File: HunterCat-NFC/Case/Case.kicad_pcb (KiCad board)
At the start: 2 copper layers, 209.4 x 35.2 mm, 4 parts

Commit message: select case
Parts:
- moved REF** 86.6 mm to (177.5, 103.8)
- moved REF** 86.3 mm to (177.2, 77.5)
- moved REF** 37.6 mm to (252.9, 77.2)
- moved REF** 36.9 mm to (252.3, 103.6)
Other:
- board size 209.4 x 35.2 mm -> 84.9 x 34.5 mm
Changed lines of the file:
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@@
-(kicad_pcb (version 20171130) (host pcbnew "(5.1.6)-1")
+(kicad_pcb (version 20171130) (host pcbnew "(5.1.5-0-10_14)")
   (general
     (thickness 1.6)
-    (drawings 44)
+    (drawings 34)
     (tracks 2)
     (zones 0)
@@
     (43 Eco2.User user)
     (44 Edge.Cuts user)
-    (45 Margin user hide)
+    (45 Margin user)
     (46 B.CrtYd user)
     (47 F.CrtYd user)
@@
   )
   (module MountingHole:MountingHole_3.2mm_M3 (layer F.Cu)
-    (at 90.91 79.29)
-    (descr "Mounting Hole 3.2mm, no annular, M3")
-    (tags "mounting hole 3.2mm no annular m3")
-    (attr virtual)
-    (fp_text reference REF** (at 0 -4.2) (layer F.Fab)
-      (effects (font (size 1 1) (thickness 0.15)))
-    )
-    (fp_text value MountingHole_3.2mm_M3 (at 0 4.2) (layer F.Fab)
-      (effects (font (size 1 1) (thickness 0.15)))
-    )
-    (fp_circle (center 0 0) (end 3.45 0) (layer F.CrtYd) (width 0.05))
-    (fp_circle (center 0 0) (end 3.2 0) (layer Cmts.User) (width 0.15))
-    (fp_text user %R (at 0.3 0) (layer F.Fab)
-      (effects (font (size 1 1) (thickness 0.15)))
-    )
-    (pad 1 np_thru_hole circle (at 0 0) (size 3.2 3.2) (drill 3.2) (layers *.Cu *.Mask))
-  )
-  (module MountingHole:MountingHole_3.2mm_M3 (layer F.Cu)
-    (at 90.91 102.76)
-    (descr "Mounting Hole 3.2mm, no annular, M3")
-    (tags "mounting hole 3.2mm no annular m3")
-    (attr virtual)
-    (fp_text reference REF** (at 0 -4.2) (layer F.Fab)
-      (effects (font (size 1 1) (thickness 0.15)))
-    )
-    (fp_text value MountingHole_3.2mm_M3 (at 0 4.2) (layer F.Fab)
-      (effects (font (size 1 1) (thickness 0.15)))
-    )
-    (fp_circle (center 0 0) (end 3.45 0) (layer F.CrtYd) (width 0.05))
-    (fp_circle (center 0 0) (end 3.2 0) (layer Cmts.User) (width 0.15))
-    (fp_text user %R (at 0.3 0) (layer F.Fab)
-      (effects (font (size 1 1) (thickness 0.15)))
-    )
-    (pad 1 np_thru_hole circle (at 0 0) (size 3.2 3.2) (drill 3.2) (layers *.Cu *.Mask))
-  )
-  (module MountingHole:MountingHole_3.2mm_M3 (layer F.Cu)
-    (at 215.42 102.08)
-    (descr "Mounting Hole 3.2mm, no annular, M3")
-    (tags "mounting hole 3.2mm no annular m3")
-    (attr virtual)
-    (fp_text reference REF** (at 0 -4.2) (layer F.Fab)
-      (effects (font (size 1 1) (thickness 0.15)))
-    )
-    (fp_text value MountingHole_3.2mm_M3 (at 0 4.2) (layer F.Fab)
-      (effects (font (size 1 1) (thickness 0.15)))
-    )
-    (fp_text user %R (at 0.3 0) (layer F.Fab)
-      (effects (font (size 1 1) (thickness 0.15)))
-    )
-    (fp_circle (center 0 0) (end 3.2 0) (layer Cmts.User) (width 0.15))
-    (fp_circle (center 0 0) (end 3.45 0) (layer F.CrtYd) (width 0.05))
-    (pad 1 np_thru_hole circle (at 0 0) (size 3.2 3.2) (drill 3.2) (layers *.Cu *.Mask))
-  )
-  (module MountingHole:MountingHole_3.2mm_M3 (layer F.Cu)
-    (at 215.42 78.61)
-    (descr "Mounting Hole 3.2mm, no annular, M3")
-    (tags "mounting hole 3.2mm no annular m3")
-    (attr virtual)
-    (fp_text reference REF** (at 0 -4.2) (layer F.Fab)
-      (effects (font (size 1 1) (thickness 0.15)))
-    )
-    (fp_text value MountingHole_3.2mm_M3 (at 0 4.2) (layer F.Fab)
-      (effects (font (size 1 1) (thickness 0.15)))
-    )
-    (fp_text user %R (at 0.3 0) (layer F.Fab)
-      (effects (font (size 1 1) (thickness 0.15)))
-    )
-    (fp_circle (center 0 0) (end 3.2 0) (layer Cmts.User) (width 0.15))
-    (fp_circle (center 0 0) (end 3.45 0) (layer F.CrtYd) (width 0.05))
-    (pad 1 np_thru_hole circle (at 0 0) (size 3.2 3.2) (drill 3.2) (layers *.Cu *.Mask))
-  )
-  (gr_line (start 60.26 73.79) (end 70.27 73.79) (layer Edge.Cuts) (width 0.05))
-  (gr_arc (start 52.06 104.29) (end 48.06 104.29) (angle -90) (layer Edge.Cuts) (width 0.05))
-  (gr_arc (start 128.95 77.79) (end 132.95 77.79) (angle -90) (layer Edge.Cuts) (width 0.05))
-  (gr_arc (start 128.95 104.29) (end 128.959999 108.289999) (angle -90) (layer Edge.Cuts) (width 0.05))
-  (gr_line (start 52.06 108.29) (end 128.959999 108.289999) (layer Edge.Cuts) (width 0.05))
-  (gr_line (start 128.95 73.79) (end 70.27 73.79) (layer Edge.Cuts) (width 0.05))
-  (gr_line (start 132.949999 104.280001) (end 132.95 77.79) (layer Edge.Cuts) (width 0.05))
-  (gr_arc (start 52.05 77.78) (end 52.05 73.79) (angle -90) (layer Edge.Cuts) (width 0.05))
-  (gr_line (start 48.06 104.29) (end 48.06 77.78) (layer Edge.Cuts) (width 0.05))
-  (gr_line (start 60.26 73.79) (end 52.05 73.79) (layer Edge.Cuts) (width 0.05))
+    (at 177.24 77.46)
+    (descr "Mounting Hole 3.2mm, no annular, M3")
+    (tags "mounting hole 3.2mm no annular m3")
+    (attr virtual)
+    (fp_text reference REF** (at 0 -4.2) (layer F.Fab)
+      (effects (font (size 1 1) (thickness 0.15)))
+    )
+    (fp_text value MountingHole_3.2mm_M3 (at 0 4.2) (layer F.Fab)
+      (effects (font (size 1 1) (thickness 0.15)))
+    )
+    (fp_circle (center 0 0) (end 3.45 0) (layer F.CrtYd) (width 0.05))
+    (fp_circle (center 0 0) (end 3.2 0) (layer Cmts.User) (width 0.15))
+    (fp_text user %R (at 0.3 0) (layer F.Fab)
+      (effects (font (size 1 1) (thickness 0.15)))
+    )
+    (pad 1 np_thru_hole circle (at 0 0) (size 3.2 3.2) (drill 3.2) (layers *.Cu *.Mask))
+  )
+  (module MountingHole:MountingHole_3.2mm_M3 (layer F.Cu)
+    (at 177.46 103.8)
+    (descr "Mounting Hole 3.2mm, no annular, M3")
+    (tags "mounting hole 3.2mm no annular m3")
+    (attr virtual)
+    (fp_text reference REF** (at 0 -4.2) (layer F.Fab)
+      (effects (font (size 1 1) (thickness 0.15)))
+    )
+    (fp_text value MountingHole_3.2mm_M3 (at 0 4.2) (layer F.Fab)
+      (effects (font (size 1 1) (thickness 0.15)))
+    )
+    (fp_circle (center 0 0) (end 3.45 0) (layer F.CrtYd) (width 0.05))
+    (fp_circle (center 0 0) (end 3.2 0) (layer Cmts.User) (width 0.15))
+    (fp_text user %R (at 0.3 0) (layer F.Fab)
+      (effects (font (size 1 1) (thickness 0.15)))
+    )
+    (pad 1 np_thru_hole circle (at 0 0) (size 3.2 3.2) (drill 3.2) (layers *.Cu *.Mask))
+  )
+  (module MountingHole:MountingHole_3.2mm_M3 (layer F.Cu)
+    (at 252.28 103.58)
+    (descr "Mounting Hole 3.2mm, no annular, M3")
+    (tags "mounting hole 3.2mm no annular m3")
+    (attr virtual)
+    (fp_text reference REF** (at 0 -4.2) (layer F.Fab)
+      (effects (font (size 1 1) (thickness 0.15)))
+    )
+    (fp_text value MountingHole_3.2mm_M3 (at 0 4.2) (layer F.Fab)
+      (effects (font (size 1 1) (thickness 0.15)))
+    )
+    (fp_text user %R (at 0.3 0) (layer F.Fab)
+      (effects (font (size 1 1) (thickness 0.15)))
+    )
+    (fp_circle (center 0 0) (end 3.2 0) (layer Cmts.User) (width 0.15))
+    (fp_circle (center 0 0) (end 3.45 0) (layer F.CrtYd) (width 0.05))
+    (pad 1 np_thru_hole circle (at 0 0) (size 3.2 3.2) (drill 3.2) (layers *.Cu *.Mask))
+  )
+  (module MountingHole:MountingHole_3.2mm_M3 (layer F.Cu)
+    (at 252.95 77.23)
+    (descr "Mounting Hole 3.2mm, no annular, M3")
+    (tags "mounting hole 3.2mm no annular m3")
+    (attr virtual)
+    (fp_text reference REF** (at 0 -4.2) (layer F.Fab)
+      (effects (font (size 1 1) (thickness 0.15)))
+    )
+    (fp_text value MountingHole_3.2mm_M3 (at 0 4.2) (layer F.Fab)
+      (effects (font (size 1 1) (thickness 0.15)))
+    )
+    (fp_text user %R (at 0.3 0) (layer F.Fab)
+      (effects (font (size 1 1) (thickness 0.15)))
+    )
+    (fp_circle (center 0 0) (end 3.2 0) (layer Cmts.User) (width 0.15))
+    (fp_circle (center 0 0) (end 3.45 0) (layer F.CrtYd) (width 0.05))
+    (pad 1 np_thru_hole circle (at 0 0) (size 3.2 3.2) (drill 3.2) (layers *.Cu *.Mask))
+  )
   (dimension 5.5 (width 0.12) (layer Margin)
     (gr_text "5,500 mm" (at 285.49 104.86 90) (layer Margin)
@@
   )
   (dimension 50.760001 (width 0.12) (layer Margin)
-    (gr_text "50,760 mm" (at 232.06384 162.504943 360) (layer Margin)
-      (effects (font (size 1 1) (thickness 0.15)))
-    )
+    (gr_text "50,760 mm" (at 232.06384 162.504943) (layer Margin)
+      (effects (font (size 1 1) (thickness 0.15)))
+    )

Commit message: New Case
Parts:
- removed the REF** at (177.2, 77.5)
- removed the REF** at (177.5, 103.8)
- removed the REF** at (252.3, 103.6)
- removed the REF** at (252.9, 77.2)
- added REF**: MountingHole_2.2mm_M2, MountingHole:MountingHole_2.2mm_M2, F.Cu at (106.6, 143.0)
- added REF**: MountingHole_2.2mm_M2, MountingHole:MountingHole_2.2mm_M2, F.Cu at (188.5, 78.4)
- added REF**: MountingHole_2.2mm_M2, MountingHole:MountingHole_2.2mm_M2, F.Cu at (187.6, 143.0)
- added REF**: MountingHole_2.2mm_M2, MountingHole:MountingHole_2.2mm_M2, F.Cu at (187.8, 115.3)
- added REF**: MountingHole_2.2mm_M2, MountingHole:MountingHole_2.2mm_M2, F.Cu at (106.6, 115.3)
- added REF**: MountingHole_2.2mm_M2, MountingHole:MountingHole_2.2mm_M2, F.Cu at (138.2, 82.7)
- added REF**: MountingHole_2.2mm_M2, MountingHole:MountingHole_2.2mm_M2, F.Cu at (138.2, 104.0)
- added REF**: MountingHole_2.2mm_M2, MountingHole:MountingHole_2.2mm_M2, F.Cu at (107.3, 106.1)
- added REF**: MountingHole_2.2mm_M2, MountingHole:MountingHole_2.2mm_M2, F.Cu at (107.3, 78.4)
- added REF**: MountingHole_2.2mm_M2, MountingHole:MountingHole_2.2mm_M2, F.Cu at (188.2, 106.1)
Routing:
- net (no net): vias 2 -> 0
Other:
- board size 84.9 x 34.5 mm -> 88.7 x 70.4 mm

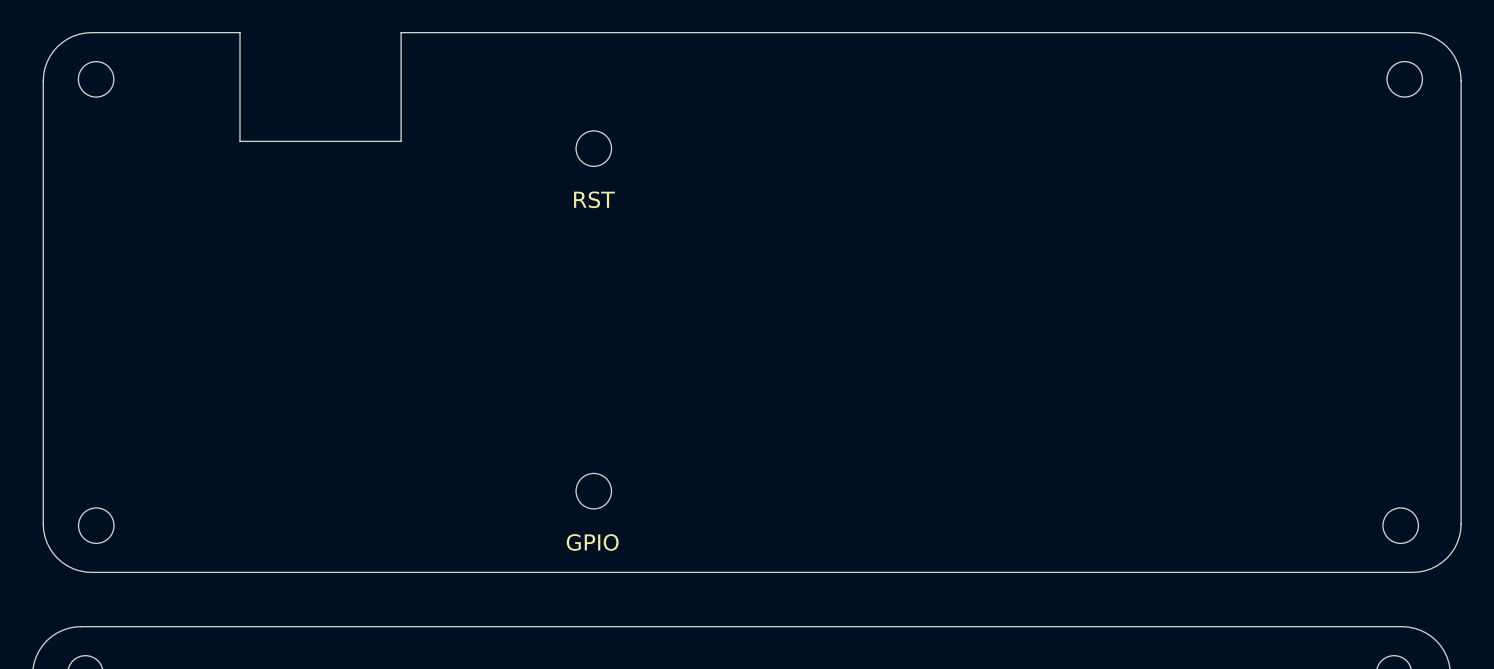
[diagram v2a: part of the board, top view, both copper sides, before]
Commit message: Add button
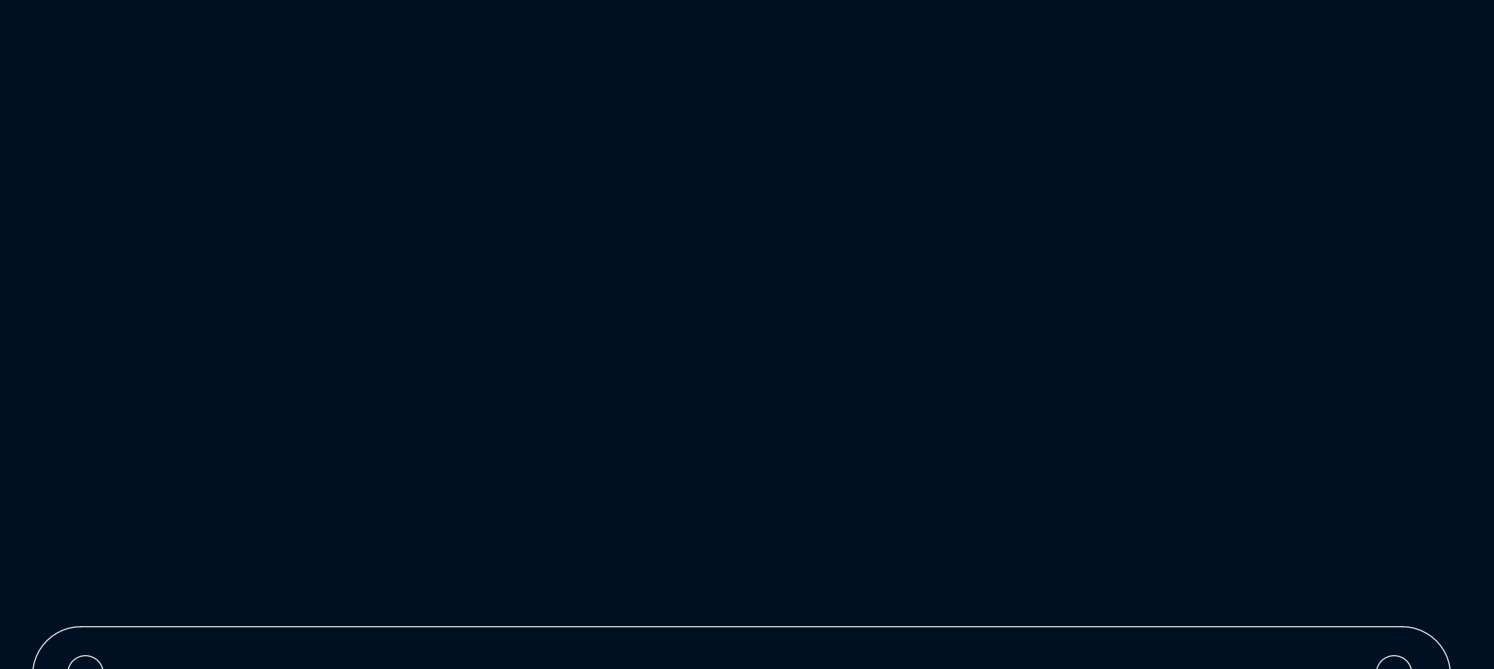
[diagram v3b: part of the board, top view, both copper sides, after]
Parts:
- removed the REF** at (188.5, 78.4)
- removed the REF** at (138.2, 82.7)
- removed the REF** at (138.2, 104.0)
- removed the REF** at (107.3, 106.1)
- removed the REF** at (107.3, 78.4)
- removed the REF** at (188.2, 106.1)
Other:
- board size 88.7 x 70.4 mm -> 88 x 33.5 mm
- board text removed: "GPIO"
- board text removed: "RST"
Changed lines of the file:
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@@
   (general
     (thickness 1.6)
-    (drawings 25)
+    (drawings 11)
     (tracks 0)
     (zones 0)
-    (modules 10)
+    (modules 4)
     (nets 1)
   )
@@
       (effects (font (size 1 1) (thickness 0.15)))
     )
-    (fp_text user %R (at 0.3 0) (layer F.Fab)
-      (effects (font (size 1 1) (thickness 0.15)))
-    )
-    (fp_circle (center 0 0) (end 2.2 0) (layer Cmts.User) (width 0.15))
-    (fp_circle (center 0 0) (end 2.45 0) (layer F.CrtYd) (width 0.05))
+    (fp_circle (center 0 0) (end 2.45 0) (layer F.CrtYd) (width 0.05))
+    (fp_circle (center 0 0) (end 2.2 0) (layer Cmts.User) (width 0.15))
+    (fp_text user %R (at 0.3 0) (layer F.Fab)
+      (effects (font (size 1 1) (thickness 0.15)))
+    )
     (pad 1 np_thru_hole circle (at 0 0) (size 2.2 2.2) (drill 2.2) (layers *.Cu *.Mask))
   )
@@
       (effects (font (size 1 1) (thickness 0.15)))
     )
-    (fp_text user %R (at 0.3 0) (layer F.Fab)
-      (effects (font (size 1 1) (thickness 0.15)))
-    )
-    (fp_circle (center 0 0) (end 2.2 0) (layer Cmts.User) (width 0.15))
-    (fp_circle (center 0 0) (end 2.45 0) (layer F.CrtYd) (width 0.05))
+    (fp_circle (center 0 0) (end 2.45 0) (layer F.CrtYd) (width 0.05))
+    (fp_circle (center 0 0) (end 2.2 0) (layer Cmts.User) (width 0.15))
+    (fp_text user %R (at 0.3 0) (layer F.Fab)
+      (effects (font (size 1 1) (thickness 0.15)))
+    )
     (pad 1 np_thru_hole circle (at 0 0) (size 2.2 2.2) (drill 2.2) (layers *.Cu *.Mask))
   )
@@
       (effects (font (size 1 1) (thickness 0.15)))
     )
-    (fp_circle (center 0 0) (end 2.45 0) (layer F.CrtYd) (width 0.05))
-    (fp_circle (center 0 0) (end 2.2 0) (layer Cmts.User) (width 0.15))
+    (fp_circle (center 0 0) (end 2.2 0) (layer Cmts.User) (width 0.15))
+    (fp_circle (center 0 0) (end 2.45 0) (layer F.CrtYd) (width 0.05))
     (fp_text user %R (at 0.3 0) (layer F.Fab)
       (effects (font (size 1 1) (thickness 0.15)))
@@
       (effects (font (size 1 1) (thickness 0.15)))
     )
-    (fp_circle (center 0 0) (end 2.45 0) (layer F.CrtYd) (width 0.05))
-    (fp_circle (center 0 0) (end 2.2 0) (layer Cmts.User) (width 0.15))
-    (fp_text user %R (at 0.3 0) (layer F.Fab)
-      (effects (font (size 1 1) (thickness 0.15)))
-    )
-    (pad 1 np_thru_hole circle (at 0 0) (size 2.2 2.2) (drill 2.2) (layers *.Cu *.Mask))
-  )
-  (module MountingHole:MountingHole_2.2mm_M2 (layer F.Cu)
-    (at 138.17 82.7)
-    (descr "Mounting Hole 2.2mm, no annular, M2")
-    (tags "mounting hole 2.2mm no annular m2")
-    (attr virtual)
-    (fp_text reference REF** (at 0 -3.2) (layer F.Fab)
-      (effects (font (size 1 1) (thickness 0.15)))
-    )
-    (fp_text value MountingHole_2.2mm_M2 (at 0 3.2) (layer F.Fab)
-      (effects (font (size 1 1) (thickness 0.15)))
-    )
-    (fp_text user %R (at 0.3 0) (layer F.Fab)
-      (effects (font (size 1 1) (thickness 0.15)))
-    )
-    (fp_circle (center 0 0) (end 2.2 0) (layer Cmts.User) (width 0.15))
-    (fp_circle (center 0 0) (end 2.45 0) (layer F.CrtYd) (width 0.05))
-    (pad 1 np_thru_hole circle (at 0 0) (size 2.2 2.2) (drill 2.2) (layers *.Cu *.Mask))
-  )
-  (module MountingHole:MountingHole_2.2mm_M2 (layer F.Cu)
-    (at 138.17 103.96)
-    (descr "Mounting Hole 2.2mm, no annular, M2")
-    (tags "mounting hole 2.2mm no annular m2")
-    (attr virtual)
-    (fp_text reference REF** (at 0 -3.2) (layer F.Fab)
-      (effects (font (size 1 1) (thickness 0.15)))
-    )
-    (fp_text value MountingHole_2.2mm_M2 (at 0 3.2) (layer F.Fab)
-      (effects (font (size 1 1) (thickness 0.15)))
-    )
-    (fp_circle (center 0 0) (end 2.45 0) (layer F.CrtYd) (width 0.05))
-    (fp_circle (center 0 0) (end 2.2 0) (layer Cmts.User) (width 0.15))
-    (fp_text user %R (at 0.3 0) (layer F.Fab)
-      (effects (font (size 1 1) (thickness 0.15)))
-    )
-    (pad 1 np_thru_hole circle (at 0 0) (size 2.2 2.2) (drill 2.2) (layers *.Cu *.Mask))
-  )
-  (module MountingHole:MountingHole_2.2mm_M2 (layer F.Cu)
-    (at 107.29 106.1)
-    (descr "Mounting Hole 2.2mm, no annular, M2")
-    (tags "mounting hole 2.2mm no annular m2")
-    (attr virtual)
-    (fp_text reference REF** (at 0 -3.2) (layer F.Fab)
-      (effects (font (size 1 1) (thickness 0.15)))
-    )
-    (fp_text value MountingHole_2.2mm_M2 (at 0 3.2) (layer F.Fab)
-      (effects (font (size 1 1) (thickness 0.15)))
-    )
-    (fp_circle (center 0 0) (end 2.45 0) (layer F.CrtYd) (width 0.05))
-    (fp_circle (center 0 0) (end 2.2 0) (layer Cmts.User) (width 0.15))
-    (fp_text user %R (at 0.3 0) (layer F.Fab)
-      (effects (font (size 1 1) (thickness 0.15)))
-    )
-    (pad 1 np_thru_hole circle (at 0 0) (size 2.2 2.2) (drill 2.2) (layers *.Cu *.Mask))
-  )
-  (module MountingHole:MountingHole_2.2mm_M2 (layer F.Cu)
-    (at 107.28 78.4)
-    (descr "Mounting Hole 2.2mm, no annular, M2")
-    (tags "mounting hole 2.2mm no annular m2")
-    (attr virtual)
-    (fp_text reference REF** (at 0 -3.2) (layer F.Fab)
-      (effects (font (size 1 1) (thickness 0.15)))
-    )
-    (fp_text value MountingHole_2.2mm_M2 (at 0 3.2) (layer F.Fab)
-      (effects (font (size 1 1) (thickness 0.15)))
-    )
-    (fp_text user %R (at 0.3 0) (layer F.Fab)
-      (effects (font (size 1 1) (thickness 0.15)))
-    )
-    (fp_circle (center 0 0) (end 2.2 0) (layer Cmts.User) (width 0.15))
-    (fp_circle (center 0 0) (end 2.45 0) (layer F.CrtYd) (width 0.05))
-    (pad 1 np_thru_hole circle (at 0 0) (size 2.2 2.2) (drill 2.2) (layers *.Cu *.Mask))
-  )
-  (module MountingHole:MountingHole_2.2mm_M2 (layer F.Cu)
-    (at 188.25 106.1)
-    (descr "Mounting Hole 2.2mm, no annular, M2")
-    (tags "mounting hole 2.2mm no annular m2")
-    (attr virtual)
-    (fp_text reference REF** (at 0 -3.2) (layer F.Fab)
-      (effects (font (size 1 1) (thickness 0.15)))
-    )
-    (fp_text value MountingHole_2.2mm_M2 (at 0 3.2) (layer F.Fab)
-      (effects (font (size 1 1) (thickness 0.15)))
-    )
-    (fp_circle (center 0 0) (end 2.45 0) (layer F.CrtYd) (width 0.05))
-    (fp_circle (center 0 0) (end 2.2 0) (layer Cmts.User) (width 0.15))
-    (fp_text user %R (at 0.3 0) (layer F.Fab)
-      (effects (font (size 1 1) (thickness 0.15)))
-    )
-    (pad 1 np_thru_hole circle (at 0 0) (size 2.2 2.2) (drill 2.2) (layers *.Cu *.Mask))
-  )
-  (module MountingHole:MountingHole_2.2mm_M2 (layer F.Cu)
-    (at 188.5 78.4)
-    (descr "Mounting Hole 2.2mm, no annular, M2")
-    (tags "mounting hole 2.2mm no annular m2")
-    (attr virtual)
-    (fp_text reference REF** (at 0 -3.2) (layer F.Fab)
-      (effects (font (size 1 1) (thickness 0.15)))
-    )
-    (fp_text value MountingHole_2.2mm_M2 (at 0 3.2) (layer F.Fab)
-      (effects (font (size 1 1) (thickness 0.15)))
-    )
-    (fp_text user %R (at 0.3 0) (layer F.Fab)
-      (effects (font (size 1 1) (thickness 0.15)))
-    )
-    (fp_circle (center 0 0) (end 2.2 0) (layer Cmts.User) (width 0.15))
-    (fp_circle (center 0 0) (end 2.45 0) (layer F.CrtYd) (width 0.05))
+    (fp_circle (center 0 0) (end 2.2 0) (layer Cmts.User) (width 0.15))
+    (fp_circle (center 0 0) (end 2.45 0) (layer F.CrtYd) (width 0.05))
+    (fp_text user %R (at 0.3 0) (layer F.Fab)
+      (effects (font (size 1 1) (thickness 0.15)))
+    )
     (pad 1 np_thru_hole circle (at 0 0) (size 2.2 2.2) (drill 2.2) (layers *.Cu *.Mask))
   )
@@
     (arrow2b (pts (xy 80.51 75.5) (xy 81.096421 76.626504)))
   )
-  (gr_text GPIO (at 138.1 107.18) (layer F.SilkS)
-    (effects (font (size 1 1) (thickness 0.15)))
-  )
-  (gr_text "RST\n" (at 138.14 85.91) (layer F.SilkS)
-    (effects (font (size 1 1) (thickness 0.15)))
-  )
-  (gr_line (start 126.21 75.5) (end 189 75.5) (layer Edge.Cuts) (width 0.05))
-  (gr_line (start 126.21 82.25) (end 126.21 75.5) (layer Edge.Cuts) (width 0.05))
-  (gr_line (start 116.21 82.25) (end 126.21 82.25) (layer Edge.Cuts) (width 0.05))
-  (gr_line (start 116.21 75.5) (end 116.21 82.25) (layer Edge.Cuts) (width 0.05))
   (dimension 10 (width 0.15) (layer Margin)
     (gr_text "10,000 mm" (at 121.21 66.58) (layer Margin)
@@
   (gr_line (start 106.34 112.37) (end 188.34 112.37) (layer Edge.Cuts) (width 0.05))
   (gr_arc (start 188.34 115.37) (end 191.34 115.37) (angle -90) (layer Edge.Cuts) (width 0.05))
-  (gr_arc (start 107 106) (end 104 106) (angle -90) (layer Edge.Cuts) (width 0.05))
-  (gr_arc (start 107 78.5) (end 107 75.5) (angle -90) (layer Edge.Cuts) (width 0.05))
-  (gr_arc (start 189 78.5) (end 192 78.5) (angle -90) (layer Edge.Cuts) (width 0.05))
-  (gr_arc (start 189 106) (end 189 109) (angle -90) (layer Edge.Cuts) (width 0.05))
-  (gr_line (start 104 106) (end 104 78.5) (layer Edge.Cuts) (width 0.05))
-  (gr_line (start 189 109) (end 107 109) (layer Edge.Cuts) (width 0.05))
-  (gr_line (start 192 78.5) (end 192 106) (layer Edge.Cuts) (width 0.05))
-  (gr_line (start 107 75.5) (end 116.21 75.5) (layer Edge.Cuts) (width 0.05))
 )
